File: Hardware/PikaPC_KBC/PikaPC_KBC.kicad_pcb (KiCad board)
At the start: 2 copper layers, 101.6 x 101.6 mm, 168 parts, among them J1 DIN41612_03x32_C_Split, J2 Mini-DIN-6, J3 Mini-DIN-6, J4 Conn_02x08_Odd_Even, J5 Conn_02x03_Odd_Even, U1 8042 PS/2, U2 74F521, U3 74LS04, U4 74LS07, U5 74FCT2245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

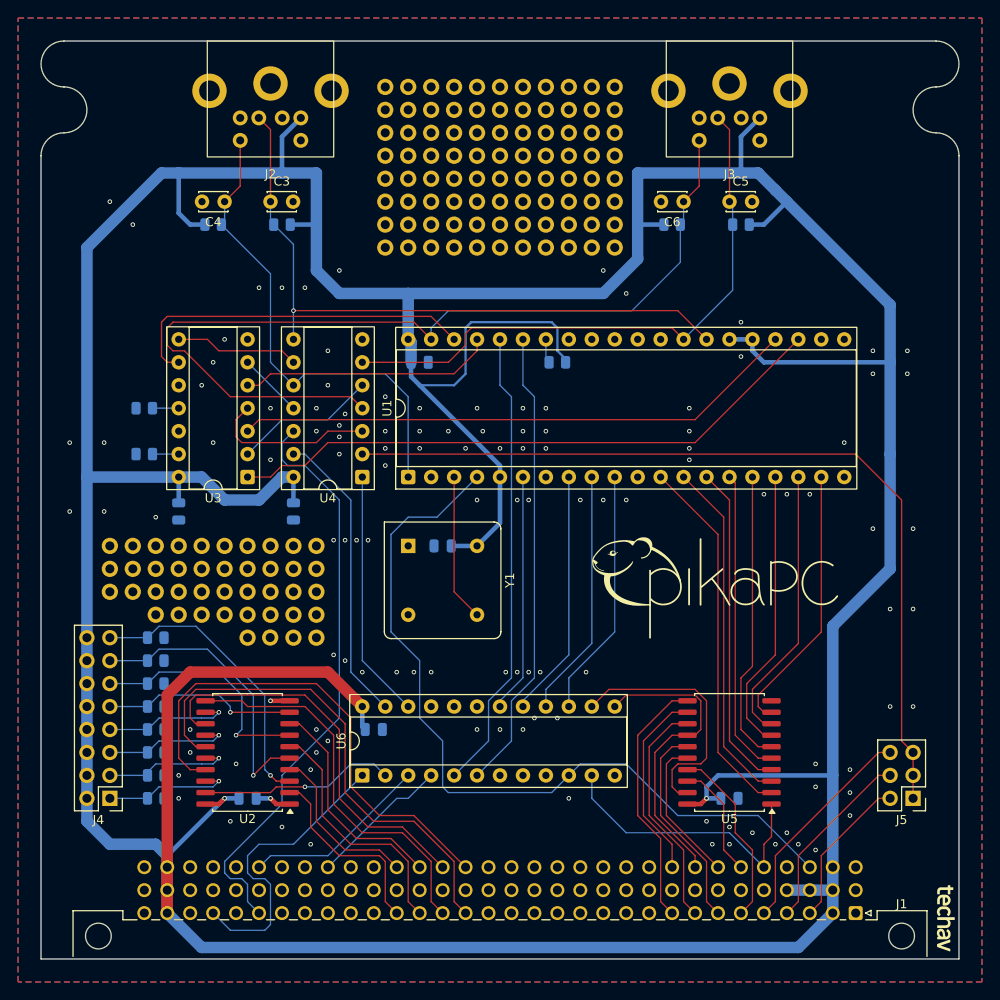
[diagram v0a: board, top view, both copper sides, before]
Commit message: Silkscreen cleanup
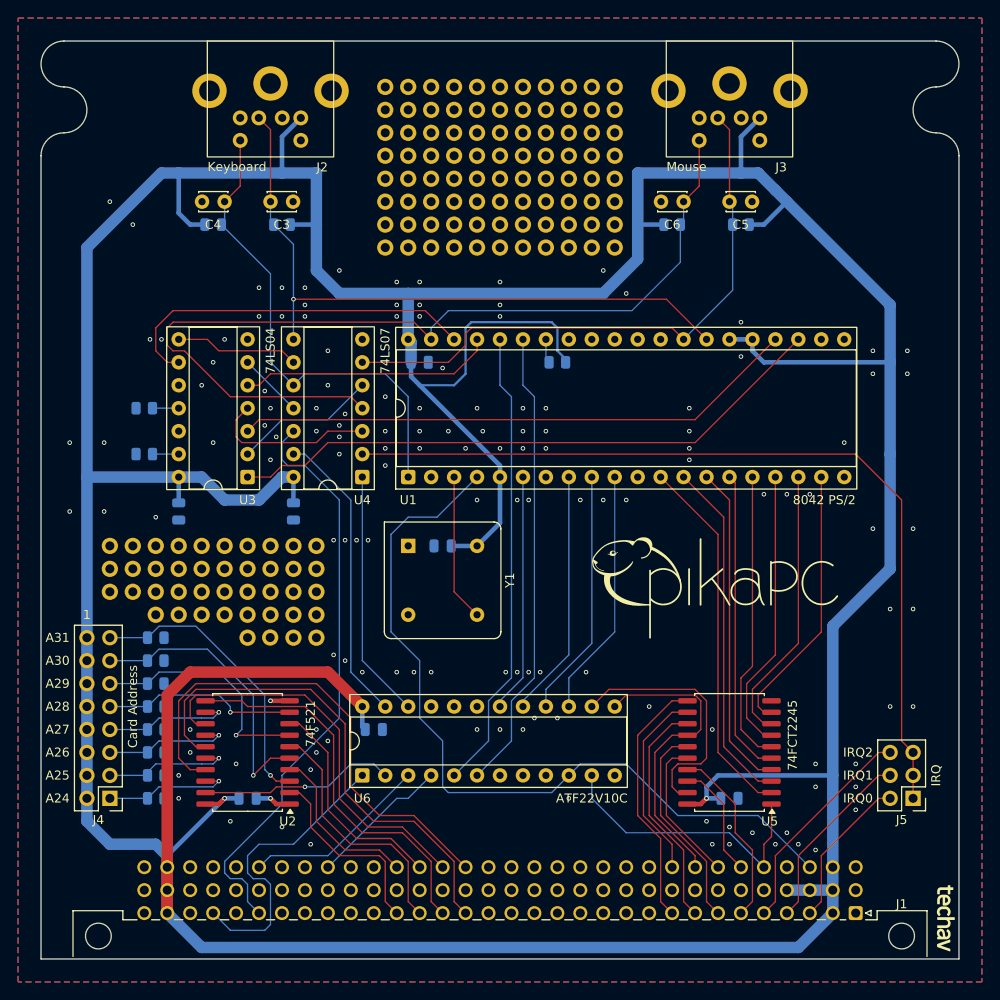
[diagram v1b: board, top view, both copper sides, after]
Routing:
- net /KBDO: track 39.7 -> 40.7 mm
- net KDAT: track 73.1 -> 73.7 mm
- net GND: vias 120 -> 141
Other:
- board text added: "1"
- board text added: "A24"
- board text added: "A25"
- board text added: "A26"
- board text added: "A27"
- board text added: "A28"
- board text added: "A29"
- board text added: "A30"
- board text added: "A31"
- board text added: "Card Address"
- board text added: "IRQ"
- board text added: "IRQ0"
- board text added: "IRQ1"
- board text added: "IRQ2"
- board text added: "Keyboard"
- board text added: "Mouse"

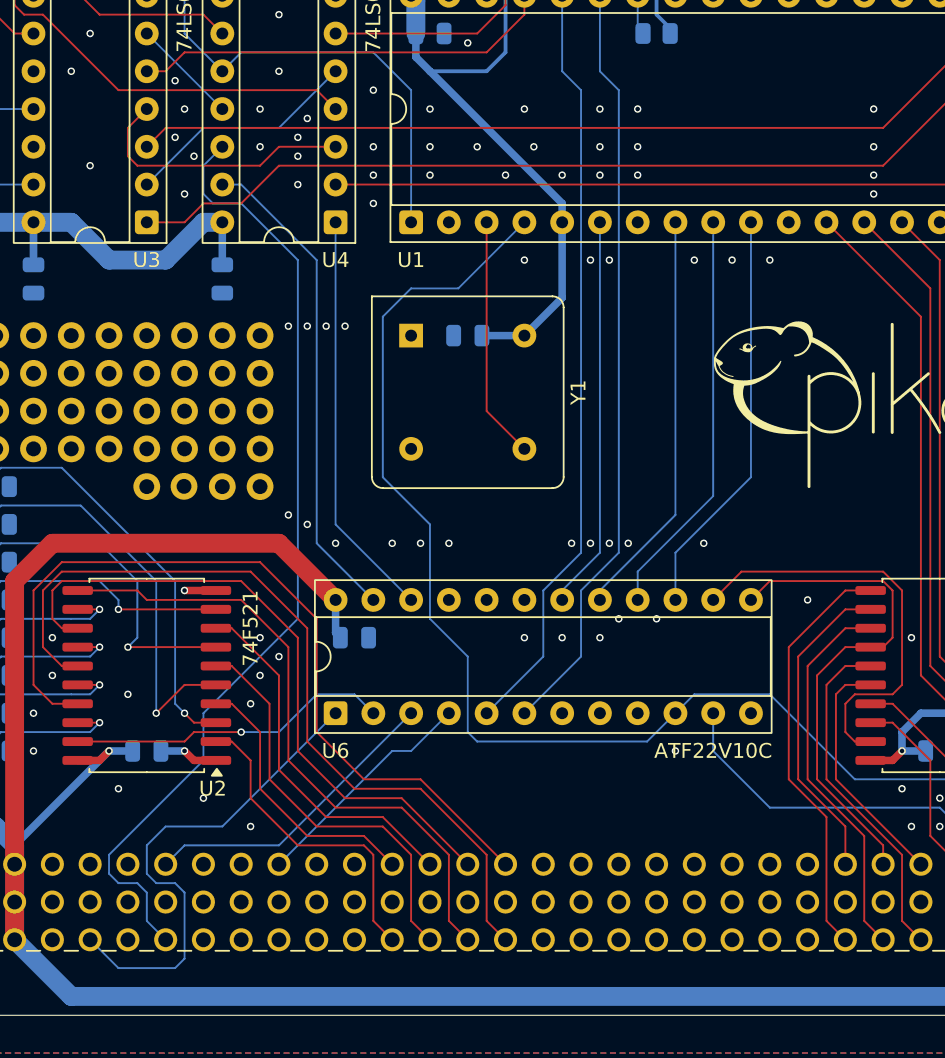
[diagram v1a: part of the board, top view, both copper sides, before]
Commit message: Annotate & prep for output - Host & KBC
add gerber output to gitignore
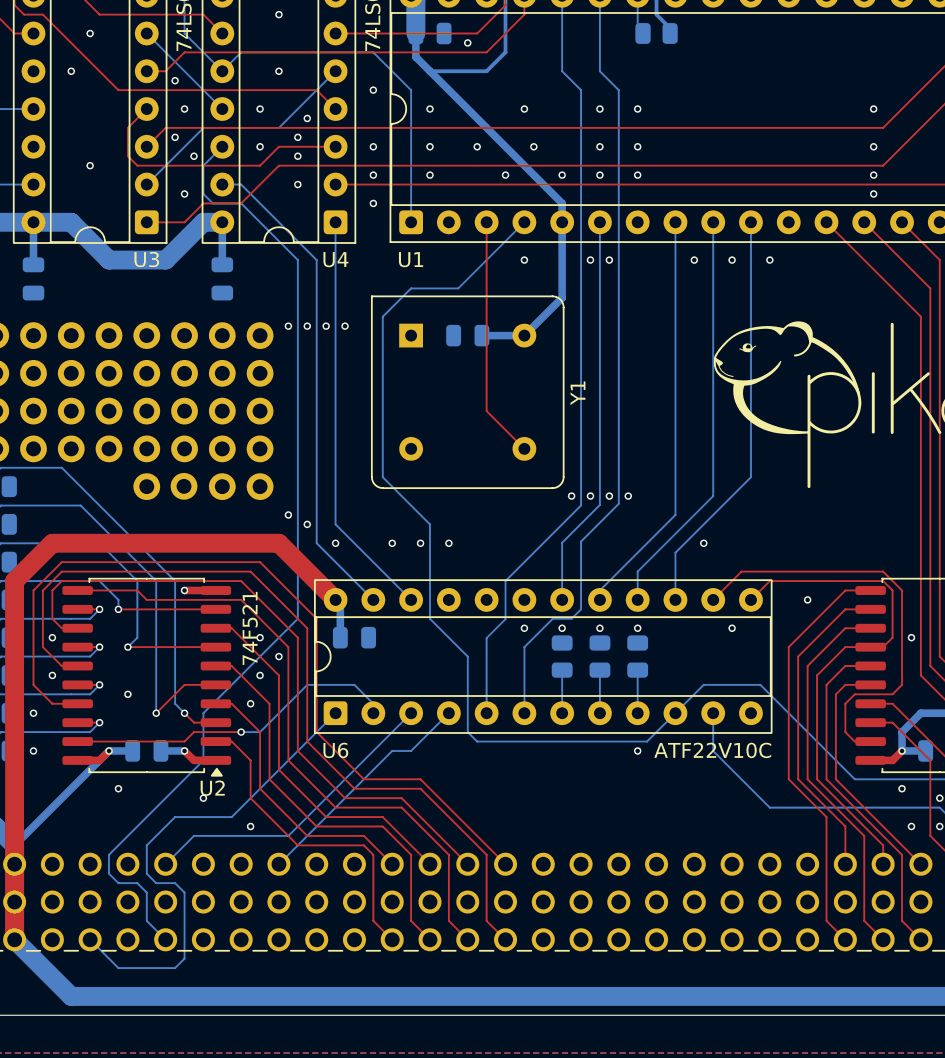
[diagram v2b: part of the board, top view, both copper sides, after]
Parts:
- added R16: 4k7, Resistor_SMD:R_0805_2012Metric, B.Cu at (127.0, 102.9)
- added R17: 4k7, Resistor_SMD:R_0805_2012Metric, B.Cu at (129.5, 102.9)
- added R18: 4k7, Resistor_SMD:R_0805_2012Metric, B.Cu at (132.1, 102.9)
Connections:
- U6 pad 7: unconnected-(U6-I5-Pad7) -> Net-(U6-I5)
- U6 pad 8: unconnected-(U6-I6-Pad8) -> Net-(U6-I6)
- U6 pad 9: unconnected-(U6-I7-Pad9) -> Net-(U6-I7)
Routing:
- net Net-(U6-I6): track 0.00 -> 2.90 mm
- net Net-(U6-I7): track 0.00 -> 2.90 mm
- net Net-(U6-I5): track 0.00 -> 2.90 mm
- net /~{ADDR}: track 21.7 -> 22.6 mm
- net /INT1: track 51.4 -> 52.2 mm
- net /~{Bus-Reset}: track 89.4 -> 89.9 mm
